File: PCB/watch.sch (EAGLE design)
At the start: 48 parts, among them IC1 ISL1209, J2 USB-MICROB, T1 BC850, U2 MKL27Z256VLH4

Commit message: added mcu caps
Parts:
- added C5, C6, C7, C8: .1uf, SparkFun:CAP0603
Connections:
- removed net PTA20: U$3.R, U2.PTA20
- new net N$2: U2.VREFL, U2.VSSA
- new net PTB16: U$3.R, U2.PTB16
- net GND: now also C5.1, C6.1, C7.1, C8.1, U2.VSS_2
- net V+: now also C5.2, C6.2, C7.2, C8.2, U2.VDD, U2.VDDA, U2.VDD_2, U2.VDD_3
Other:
- note added: "place near MCU VCC"
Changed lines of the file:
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@@
 <part name="SUPPLY9" library="supply2" deviceset="GND" device=""/>
 <part name="SUPPLY33" library="supply2" deviceset="GND" device=""/>
+<part name="SUPPLY34" library="supply2" deviceset="GND" device=""/>
+<part name="SUPPLY35" library="supply2" deviceset="V+" device=""/>
+<part name="SUPPLY36" library="supply2" deviceset="V+" device=""/>
+<part name="SUPPLY37" library="supply2" deviceset="V+" device=""/>
+<part name="C5" library="SparkFun" deviceset="CAP" device="0603" value=".1uf"/>
+<part name="C6" library="SparkFun" deviceset="CAP" device="0603" value=".1uf"/>
+<part name="C7" library="SparkFun" deviceset="CAP" device="0603" value=".1uf"/>
+<part name="SUPPLY38" library="supply2" deviceset="V+" device=""/>
+<part name="C8" library="SparkFun" deviceset="CAP" device="0603" value=".1uf"/>
+<part name="SUPPLY39" library="supply2" deviceset="V+" device=""/>
+<part name="SUPPLY40" library="supply2" deviceset="GND" device=""/>
 </parts>
 <sheets>
 <sheet>
 <plain>
+<text x="109.22" y="203.2" size="1.778" layer="91">place near MCU VCC</text>
 </plain>
 <instances>
@@
 <instance part="SUPPLY9" gate="GND" x="137.16" y="106.68" rot="R90"/>
 <instance part="SUPPLY33" gate="GND" x="147.32" y="132.08" rot="R180"/>
+<instance part="SUPPLY34" gate="GND" x="-35.56" y="154.94" rot="R270"/>
+<instance part="SUPPLY35" gate="1" x="-33.02" y="157.48" rot="R90"/>
+<instance part="SUPPLY36" gate="1" x="-43.18" y="88.9" rot="R90"/>
+<instance part="SUPPLY37" gate="1" x="91.44" y="121.92" rot="R270"/>
+<instance part="C5" gate="G$1" x="111.76" y="198.12" rot="R180"/>
+<instance part="C6" gate="G$1" x="121.92" y="198.12" rot="R180"/>
+<instance part="C7" gate="G$1" x="129.54" y="198.12" rot="R180"/>
+<instance part="SUPPLY38" gate="1" x="-35.56" y="132.08" rot="R90"/>
+<instance part="C8" gate="G$1" x="137.16" y="198.12" rot="R180"/>
+<instance part="SUPPLY39" gate="1" x="101.6" y="205.74"/>
+<instance part="SUPPLY40" gate="GND" x="101.6" y="185.42"/>
 </instances>
 <busses>
@@
 <wire x1="147.32" y1="127" x2="147.32" y2="129.54" width="0.1524" layer="91"/>
 </segment>
+<segment>
+<pinref part="U2" gate="A" pin="VSS_2"/>
+<pinref part="SUPPLY34" gate="GND" pin="GND"/>
+<wire x1="-25.4" y1="154.94" x2="-33.02" y2="154.94" width="0.1524" layer="91"/>
+</segment>
+<segment>
+<pinref part="C8" gate="G$1" pin="1"/>
+<pinref part="C7" gate="G$1" pin="1"/>
+<wire x1="137.16" y1="193.04" x2="129.54" y2="193.04" width="0.1524" layer="91"/>
+<pinref part="C6" gate="G$1" pin="1"/>
+<wire x1="129.54" y1="193.04" x2="121.92" y2="193.04" width="0.1524" layer="91"/>
+<pinref part="C5" gate="G$1" pin="1"/>
+<wire x1="121.92" y1="193.04" x2="111.76" y2="193.04" width="0.1524" layer="91"/>
+<pinref part="SUPPLY40" gate="GND" pin="GND"/>
+<wire x1="111.76" y1="193.04" x2="101.6" y2="193.04" width="0.1524" layer="91"/>
+<wire x1="101.6" y1="193.04" x2="101.6" y2="187.96" width="0.1524" layer="91"/>
+<junction x="129.54" y="193.04"/>
+<junction x="121.92" y="193.04"/>
+<junction x="111.76" y="193.04"/>
+</segment>
 </net>
 <net name="V+" class="0">
@@
 <wire x1="124.46" y1="106.68" x2="121.92" y2="106.68" width="0.1524" layer="91"/>
 </segment>
+<segment>
+<pinref part="SUPPLY35" gate="1" pin="V+"/>
+<pinref part="U2" gate="A" pin="VDD_2"/>
+<wire x1="-30.48" y1="157.48" x2="-25.4" y2="157.48" width="0.1524" layer="91"/>
+</segment>
+<segment>
+<pinref part="SUPPLY36" gate="1" pin="V+"/>
+<pinref part="U2" gate="A" pin="VDD_3"/>
+<wire x1="-40.64" y1="88.9" x2="-25.4" y2="88.9" width="0.1524" layer="91"/>
+</segment>
+<segment>
+<pinref part="U2" gate="A" pin="VDD"/>
+<pinref part="SUPPLY37" gate="1" pin="V+"/>
+<wire x1="81.28" y1="121.92" x2="88.9" y2="121.92" width="0.1524" layer="91"/>
+</segment>
+<segment>
+<pinref part="SUPPLY38" gate="1" pin="V+"/>
+<pinref part="U2" gate="A" pin="VDDA"/>
+<wire x1="-33.02" y1="132.08" x2="-25.4" y2="132.08" width="0.1524" layer="91"/>
+</segment>
+<segment>
+<pinref part="SUPPLY39" gate="1" pin="V+"/>
+<wire x1="101.6" y1="203.2" x2="101.6" y2="200.66" width="0.1524" layer="91"/>
+<pinref part="C5" gate="G$1" pin="2"/>
+<wire x1="101.6" y1="200.66" x2="111.76" y2="200.66" width="0.1524" layer="91"/>
+<pinref part="C6" gate="G$1" pin="2"/>
+<wire x1="111.76" y1="200.66" x2="121.92" y2="200.66" width="0.1524" layer="91"/>
+<pinref part="C7" gate="G$1" pin="2"/>
+<wire x1="121.92" y1="200.66" x2="129.54" y2="200.66" width="0.1524" layer="91"/>
+<pinref part="C8" gate="G$1" pin="2"/>
+<wire x1="129.54" y1="200.66" x2="137.16" y2="200.66" width="0.1524" layer="91"/>
+<junction x="111.76" y="200.66"/>
+<junction x="121.92" y="200.66"/>
+<junction x="129.54" y="200.66"/>
+</segment>
 </net>
 <net name="PTA19" class="0">
@@
 </segment>
 </net>
-<net name="PTA20" class="0">
+<net name="PTB16" class="0">
 <segment>
 <pinref part="U$3" gate="G$1" pin="R"/>
@@
 </segment>
 <segment>
-<pinref part="U2" gate="A" pin="PTA20"/>
-<wire x1="81.28" y1="86.36" x2="86.36" y2="86.36" width="0.1524" layer="91"/>
-<junction x="86.36" y="86.36"/>
+<pinref part="U2" gate="A" pin="PTB16"/>
+<wire x1="81.28" y1="99.06" x2="88.9" y2="99.06" width="0.1524" layer="91"/>
+<junction x="88.9" y="99.06"/>
 </segment>
 </net>
@@
 </segment>
 </net>
+<net name="N$2" class="0">
+<segment>
+<pinref part="U2" gate="A" pin="VSSA"/>
+<wire x1="-25.4" y1="124.46" x2="-30.48" y2="124.46" width="0.1524" layer="91"/>
+<wire x1="-30.48" y1="124.46" x2="-30.48" y2="127" width="0.1524" layer="91"/>
+<pinref part="U2" gate="A" pin="VREFL"/>
+<wire x1="-30.48" y1="127" x2="-25.4" y2="127" width="0.1524" layer="91"/>
+</segment>
+</net>

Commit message: added RTC crystal
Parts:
- added Q1: 32.768 KHz, crystal:CRYSTALTC26H
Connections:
- new net N$43: IC1.XTALI, Q1.2
- new net N$44: IC1.XTALO, Q1.1
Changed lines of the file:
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@@
 <part name="SUPPLY39" library="supply2" deviceset="V+" device=""/>
 <part name="SUPPLY40" library="supply2" deviceset="GND" device=""/>
+<part name="Q1" library="crystal" deviceset="CRYSTAL" device="TC26H" value="32.768 KHz"/>
 </parts>
 <sheets>
@@
 <instance part="SUPPLY39" gate="1" x="101.6" y="205.74"/>
 <instance part="SUPPLY40" gate="GND" x="101.6" y="185.42"/>
+<instance part="Q1" gate="G$1" x="-109.22" y="170.18"/>
 </instances>
 <busses>
@@
 </segment>
 </net>
+<net name="N$43" class="0">
+<segment>
+<pinref part="Q1" gate="G$1" pin="2"/>
+<pinref part="IC1" gate="G$1" pin="XTALI"/>
+<wire x1="-106.68" y1="170.18" x2="-101.6" y2="170.18" width="0.1524" layer="91"/>
+<wire x1="-101.6" y1="170.18" x2="-101.6" y2="157.48" width="0.1524" layer="91"/>
+</segment>
+</net>
+<net name="N$44" class="0">
+<segment>
+<pinref part="IC1" gate="G$1" pin="XTALO"/>
+<pinref part="Q1" gate="G$1" pin="1"/>
+<wire x1="-101.6" y1="154.94" x2="-111.76" y2="154.94" width="0.1524" layer="91"/>
+<wire x1="-111.76" y1="154.94" x2="-111.76" y2="170.18" width="0.1524" layer="91"/>
+</segment>
+</net>

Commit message: I think the SR clocks are now wired correctly?
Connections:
- removed net N$34: U$4.SHCP
- new net PTC0: U$4.SHCP, U$5.SHCP, U2.PTC0
- new net PTC2: U$4.STCP, U2.PTC2
- new net PTC7: U$5.STCP, U2.PTC7
- net PTB2: no longer U$4.STCP, U$5.SHCP, U$5.STCP
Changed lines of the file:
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@@
 <net name="PTB2" class="0">
-<segment>
-<pinref part="U$5" gate="G$1" pin="SHCP"/>
-<wire x1="12.7" y1="205.74" x2="2.54" y2="205.74" width="0.1524" layer="91"/>
-<wire x1="2.54" y1="205.74" x2="-27.94" y2="205.74" width="0.1524" layer="91"/>
-<wire x1="-27.94" y1="205.74" x2="-27.94" y2="259.08" width="0.1524" layer="91"/>
-<pinref part="U$4" gate="G$1" pin="STCP"/>
-<wire x1="-48.26" y1="256.54" x2="-48.26" y2="259.08" width="0.1524" layer="91"/>
-<label x="-48.26" y="264.16" size="1.778" layer="95"/>
-<wire x1="-48.26" y1="259.08" x2="-48.26" y2="266.7" width="0.1524" layer="91"/>
-<wire x1="-27.94" y1="259.08" x2="-48.26" y2="259.08" width="0.1524" layer="91"/>
-<junction x="-48.26" y="259.08"/>
-<pinref part="U$5" gate="G$1" pin="STCP"/>
-<wire x1="12.7" y1="210.82" x2="2.54" y2="210.82" width="0.1524" layer="91"/>
-<wire x1="2.54" y1="210.82" x2="2.54" y2="205.74" width="0.1524" layer="91"/>
-<junction x="2.54" y="205.74"/>
-</segment>
 <segment>
 <pinref part="U2" gate="A" pin="PTB2"/>
@@
 </segment>
 </net>
-<net name="N$34" class="0">
-<segment>
-<pinref part="U$4" gate="G$1" pin="SHCP"/>
-<wire x1="-53.34" y1="256.54" x2="-53.34" y2="266.7" width="0.1524" layer="91"/>
-<label x="-58.42" y="266.7" size="1.778" layer="95"/>
-</segment>
-</net>
 <net name="N$35" class="0">
 <segment>
@@
 </segment>
 </net>
+<net name="PTC7" class="0">
+<segment>
+<pinref part="U2" gate="A" pin="PTC7"/>
+<wire x1="81.28" y1="132.08" x2="86.36" y2="132.08" width="0.1524" layer="91"/>
+<junction x="86.36" y="132.08"/>
+</segment>
+<segment>
+<pinref part="U$5" gate="G$1" pin="STCP"/>
+<wire x1="12.7" y1="210.82" x2="5.08" y2="210.82" width="0.1524" layer="91"/>
+<label x="2.54" y="210.82" size="1.778" layer="95"/>
+</segment>
+</net>
+<net name="PTC0" class="0">
+<segment>
+<pinref part="U2" gate="A" pin="PTC0"/>
+<wire x1="81.28" y1="109.22" x2="88.9" y2="109.22" width="0.1524" layer="91"/>
+<junction x="88.9" y="109.22"/>
+</segment>
+<segment>
+<pinref part="U$4" gate="G$1" pin="SHCP"/>
+<wire x1="-53.34" y1="256.54" x2="-53.34" y2="259.08" width="0.1524" layer="91"/>
+<label x="-58.42" y="266.7" size="1.778" layer="95"/>
+<pinref part="U$5" gate="G$1" pin="SHCP"/>
+<wire x1="-53.34" y1="259.08" x2="-53.34" y2="266.7" width="0.1524" layer="91"/>
+<wire x1="12.7" y1="205.74" x2="-30.48" y2="205.74" width="0.1524" layer="91"/>
+<wire x1="-30.48" y1="205.74" x2="-30.48" y2="259.08" width="0.1524" layer="91"/>
+<wire x1="-30.48" y1="259.08" x2="-53.34" y2="259.08" width="0.1524" layer="91"/>
+<junction x="-53.34" y="259.08"/>
+</segment>
+</net>
+<net name="PTC2" class="0">
+<segment>
+<pinref part="U2" gate="A" pin="PTC2"/>
+<wire x1="81.28" y1="114.3" x2="88.9" y2="114.3" width="0.1524" layer="91"/>
+<junction x="88.9" y="114.3"/>
+</segment>
+<segment>
+<pinref part="U$4" gate="G$1" pin="STCP"/>
+<wire x1="-48.26" y1="256.54" x2="-48.26" y2="266.7" width="0.1524" layer="91"/>
+<label x="-48.26" y="264.16" size="1.778" layer="95"/>
+</segment>
+</net>

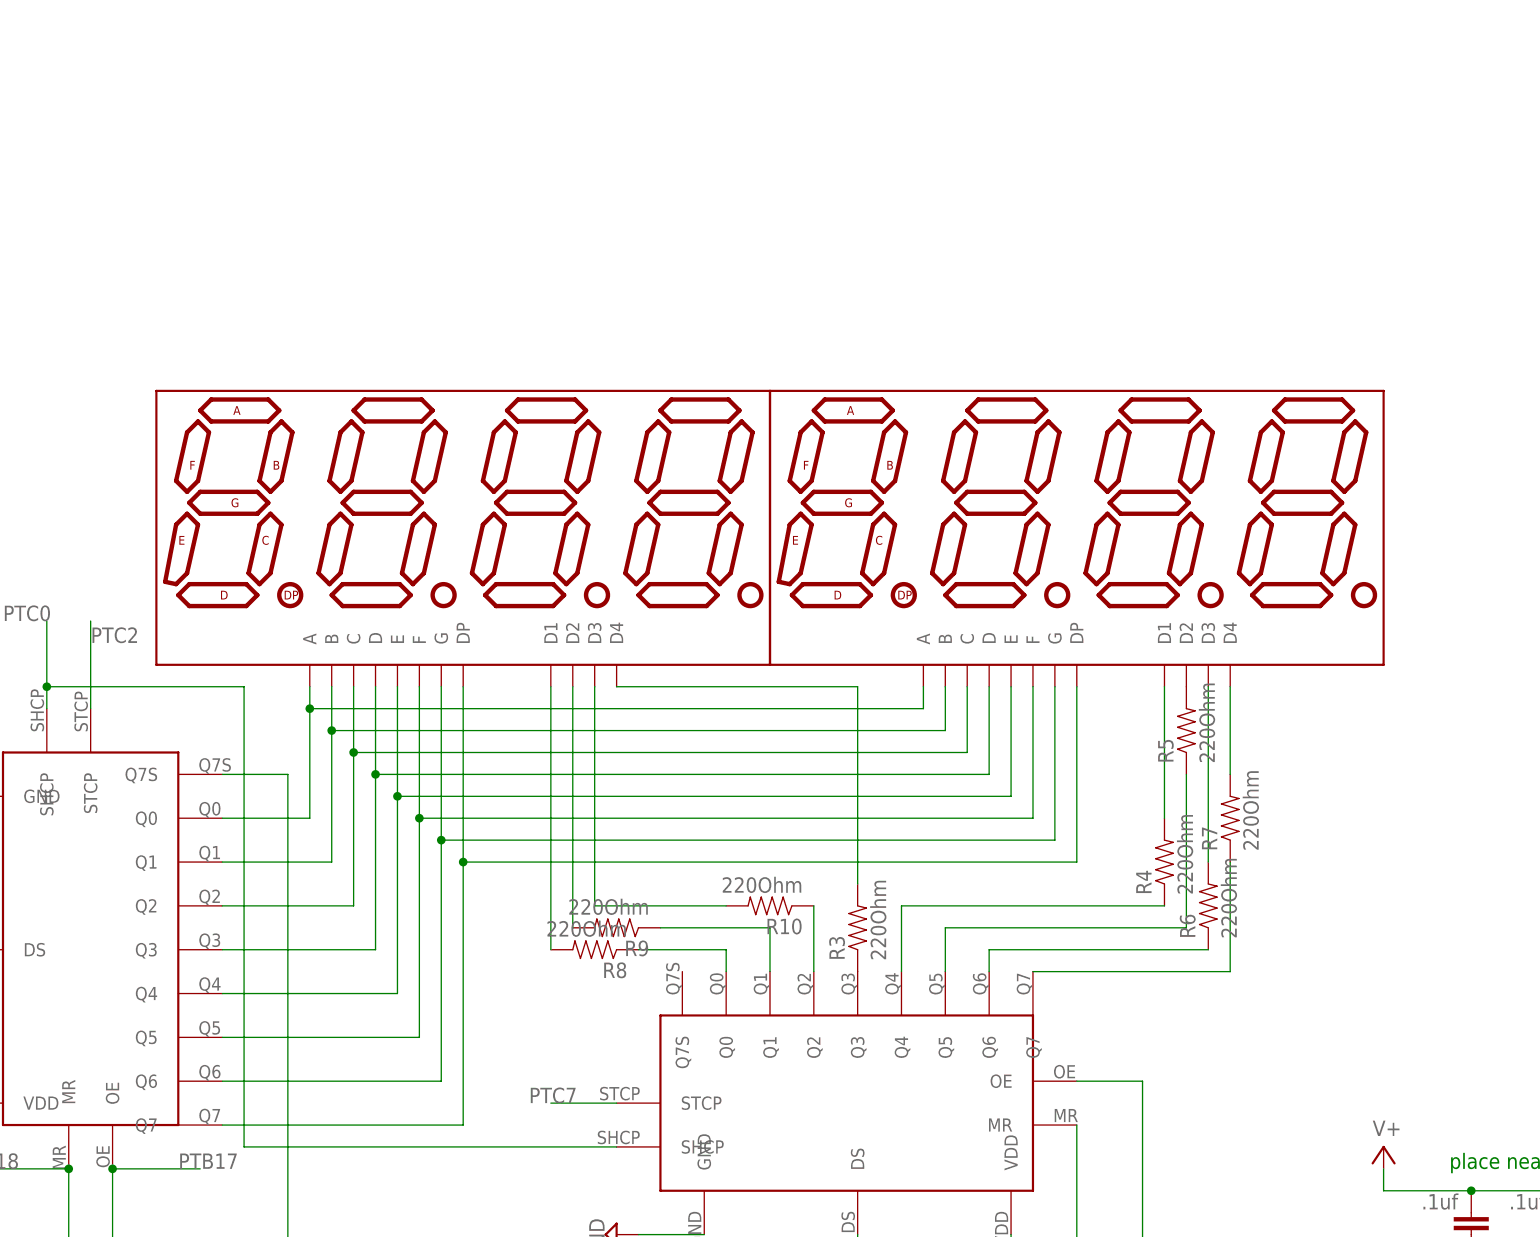
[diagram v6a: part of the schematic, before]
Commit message: Moved Resistors from digit pins to segment pins and moved README image location to private server
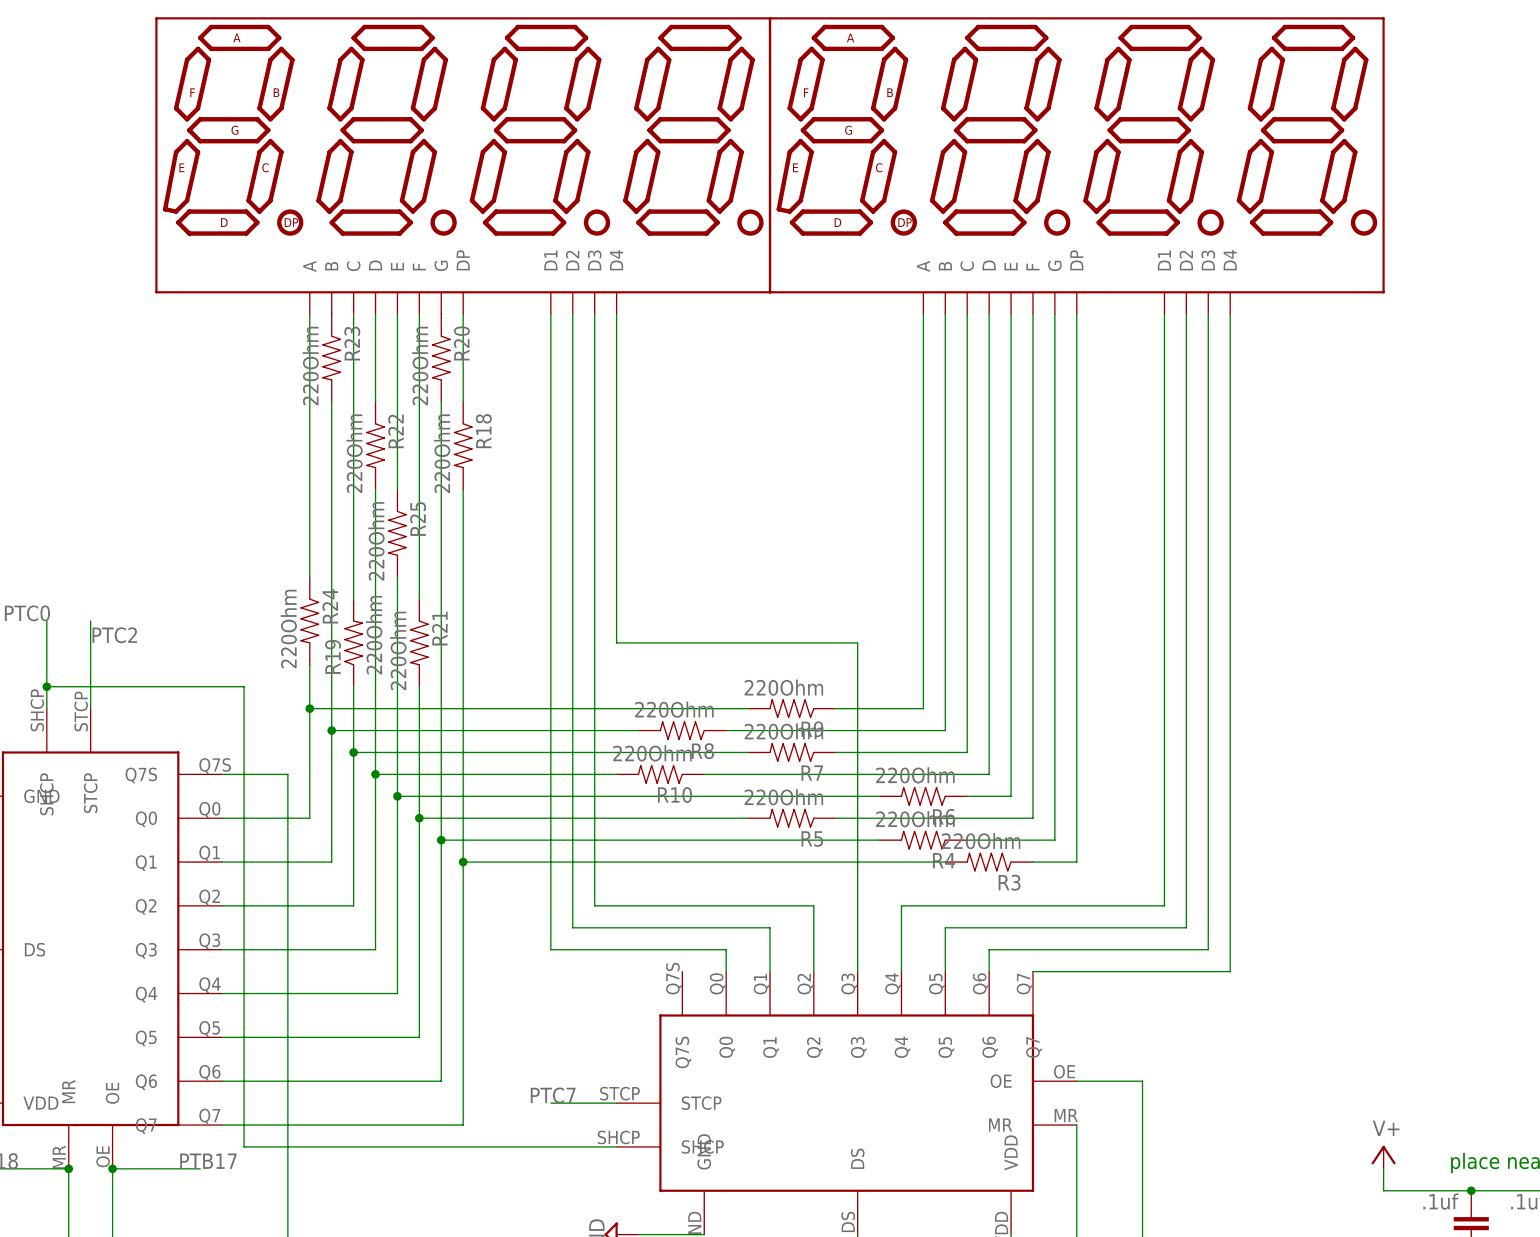
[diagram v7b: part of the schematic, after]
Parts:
- added R18, R19, R20, R21, R22, R23, R24, R25: 220Ohm, SparkFun-Resistors:RESISTOR0603
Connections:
- new net N$34: DISP1.F, R21.1
- new net N$45: DISP1.G, R20.1
- new net N$46: DISP1.DP, R18.1
- new net N$47: R25.2, R6.2, U$4.Q4
- new net N$48: DISP1.E, R25.1
- new net N$49: R19.1, R7.2, U$4.Q2
- new net N$50: R23.2, R8.2, U$4.Q1
- new net N$51: DISP1.C, R19.2
- net N$10: now also R24.2, R9.2; no longer DISP1.A, DISP2.A
- net N$11: now also DISP1.A, R24.1; no longer DISP1.B, DISP2.B, U$4.Q1
- net N$12: now also DISP1.B, R23.1; no longer DISP1.C, DISP2.C, U$4.Q2
- net N$13: now also DISP2.G, R4.1; no longer DISP2.D2, R5.2
- net N$14: now also DISP1.D, R22.1; no longer DISP1.E, DISP2.E, U$4.Q4
- net N$15: now also R21.2, R5.2; no longer DISP1.F, DISP2.F
- net N$16: now also R20.2, R4.2; no longer DISP1.G, DISP2.G
- net N$17: now also R18.2, R3.2; no longer DISP1.DP, DISP2.DP
- net N$18: now also U$5.Q6; no longer R6.2
- net N$19: now also DISP2.F, R5.1; no longer R7.1, U$5.Q7
- net N$20: now also DISP2.E; no longer U$5.Q6
- net N$21: now also R10.2, R22.2; no longer DISP1.D, DISP2.D
- net N$22: now also DISP2.D2; no longer R5.1
- net N$23: now also DISP2.D1; no longer R4.1
- net N$24: now also U$5.Q3; no longer R3.2
- net N$25: now also U$5.Q2; no longer R10.2
- net N$26: now also DISP2.D, R10.1; no longer DISP1.D2, R9.2
- net N$27: now also U$5.Q0; no longer R8.2
- net N$29: now also U$5.Q7; no longer R7.2
- net N$30: now also DISP2.C, R7.1; no longer R10.1, U$5.Q2
- net N$31: now also DISP1.D2; no longer R9.1
- net N$32: now also DISP2.B; no longer U$5.Q0
- net N$33: now also DISP2.A, R9.1; no longer R3.1, U$5.Q3
- net N$9: now also DISP2.DP, R3.1; no longer DISP2.D1, R4.2
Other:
- moved on the sheet: R10, R3, R4, R5, R6, R7, R8, R9
